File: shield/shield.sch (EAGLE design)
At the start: 23 parts, among them IC1 MCP2515-E/SO, IC2 MCP2562, IC3 LM2595NDH

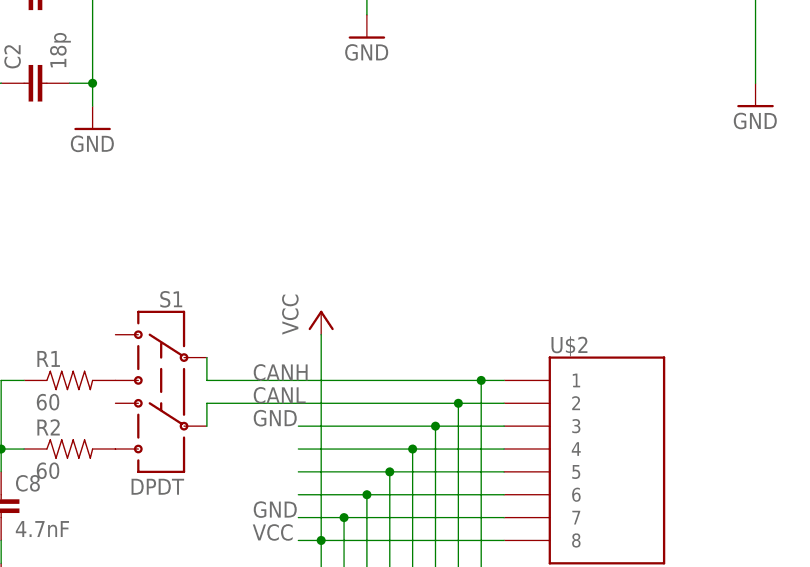
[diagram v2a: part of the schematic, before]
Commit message: Added TVS diodes, fixed silkscreen issues
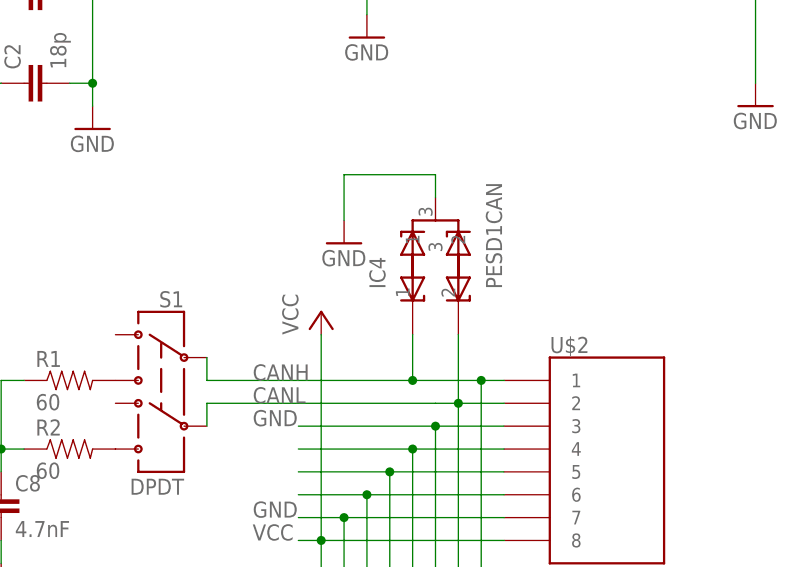
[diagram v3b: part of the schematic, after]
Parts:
- added IC4: PESD1CAN, nickparts:PESD1CAN
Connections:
- net CANH: now also IC4.1
- net CANL: now also IC4.2
- net GND: now also IC4.3
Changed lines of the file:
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@@
 <part name="C8" library="SparkFun-Passives" deviceset="CAP" device="0603-CAP" value="4.7nF"/>
 <part name="GND1" library="supply1" deviceset="GND" device=""/>
+<part name="IC4" library="nickparts" deviceset="PESD1CAN" device=""/>
+<part name="GND2" library="supply1" deviceset="GND" device=""/>
 </parts>
 <sheets>
@@
 <instance part="C8" gate="G$1" x="335.28" y="-88.9"/>
 <instance part="GND1" gate="1" x="335.28" y="-96.52"/>
+<instance part="IC4" gate="G$1" x="383.54" y="-55.88" rot="R90"/>
+<instance part="GND2" gate="1" x="373.38" y="-58.42"/>
 </instances>
 <busses>
@@
 <wire x1="335.28" y1="-91.44" x2="335.28" y2="-93.98" width="0.1524" layer="91"/>
 </segment>
+<segment>
+<pinref part="IC4" gate="G$1" pin="3"/>
+<wire x1="383.54" y1="-53.34" x2="383.54" y2="-50.8" width="0.1524" layer="91"/>
+<pinref part="GND2" gate="1" pin="GND"/>
+<wire x1="383.54" y1="-50.8" x2="373.38" y2="-50.8" width="0.1524" layer="91"/>
+<wire x1="373.38" y1="-50.8" x2="373.38" y2="-55.88" width="0.1524" layer="91"/>
+</segment>
 </net>
 <net name="N$6" class="0">
@@
 <pinref part="U$3" gate="G$1" pin="1"/>
 <wire x1="388.62" y1="-101.6" x2="391.16" y2="-101.6" width="0.1524" layer="91"/>
-<wire x1="388.62" y1="-73.66" x2="368.3" y2="-73.66" width="0.1524" layer="91"/>
+<wire x1="388.62" y1="-73.66" x2="381" y2="-73.66" width="0.1524" layer="91"/>
 <junction x="388.62" y="-73.66"/>
 <label x="363.22" y="-73.66" size="1.778" layer="95"/>
 <pinref part="S1" gate="G$1" pin="2"/>
+<wire x1="381" y1="-73.66" x2="368.3" y2="-73.66" width="0.1524" layer="91"/>
 <wire x1="368.3" y1="-73.66" x2="358.14" y2="-73.66" width="0.1524" layer="91"/>
 <wire x1="358.14" y1="-73.66" x2="358.14" y2="-71.12" width="0.1524" layer="91"/>
+<pinref part="IC4" gate="G$1" pin="1"/>
+<wire x1="381" y1="-68.58" x2="381" y2="-73.66" width="0.1524" layer="91"/>
+<junction x="381" y="-73.66"/>
 </segment>
 </net>
@@
 <pinref part="U$3" gate="G$1" pin="2"/>
 <wire x1="386.08" y1="-104.14" x2="391.16" y2="-104.14" width="0.1524" layer="91"/>
-<wire x1="386.08" y1="-76.2" x2="368.3" y2="-76.2" width="0.1524" layer="91"/>
+<wire x1="386.08" y1="-76.2" x2="383.54" y2="-76.2" width="0.1524" layer="91"/>
 <junction x="386.08" y="-76.2"/>
 <label x="363.22" y="-76.2" size="1.778" layer="95"/>
 <pinref part="S1" gate="G$1" pin="5"/>
+<wire x1="383.54" y1="-76.2" x2="368.3" y2="-76.2" width="0.1524" layer="91"/>
 <wire x1="368.3" y1="-76.2" x2="358.14" y2="-76.2" width="0.1524" layer="91"/>
 <wire x1="358.14" y1="-76.2" x2="358.14" y2="-78.74" width="0.1524" layer="91"/>
-</segment>
-</net>
+<pinref part="IC4" gate="G$1" pin="2"/>
+<wire x1="386.08" y1="-68.58" x2="386.08" y2="-76.2" width="0.1524" layer="91"/>
+</segment>
+</net>

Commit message: Minor changes to shield, rpi board, and cape
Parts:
- removed L1: MSS1260, nickparts:MSS1260
- added C10: 56u, nickparts:10SVP56M
- added C9: 10n, nickparts:C0805C103K5RACTU
- added I1: SRN8040-330M, nickparts:SRN8040-330M
- C3: value (none) -> 4.7u; device SparkFun-Capacitors:CAP_POLG -> nickparts:GRM31CR71H475KA12L
- C4: value (none) -> 1u; device SparkFun-Capacitors:CAP_POLE -> nickparts:GMK212B7105KG-T
- D1: value (none) -> B240A-13-F; device SparkFun-DiscreteSemi:DIODESMA-ALT -> nickparts:B240A-13-F
- IC3: value LM2595NDH -> LM22675MR-5.0/NOPB; device nickparts:LM2595NDH -> nickparts:LM22675MR-5.0/NOPB
- U$1: value ARDUINO_R3_ICSP -> ARDUINO_R3_ICSPNODIM; device adafruit:ARDUINO_R3_ICSP -> nickparts:ARDUINO_R3_ICSPNODIM
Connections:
- net N$1 renamed RXCAN
- removed net N$11: U$2.5, U$3.5
- removed net N$6: D1.C, IC3.OUT, L1.1
- new net N$9: U$2.3, U$3.3
- new net SWOUT: C9.2, D1.K, I1.2, IC3.SW
- net +5V: now also C10.+, I1.1; no longer C4.+, L1.2
- net GND: now also C10.-, C3.2, C4.2, U$2.8, U$3.8; no longer C3.-, C4.-, IC3./EN, U$2.3, U$3.3
- net N$10: now also C9.1, IC3.BOOT; no longer U$2.4, U$3.4
- net VCC: now also C3.1, C4.1, U$2.4, U$2.5, U$3.4, U$3.5; no longer C3.+, U$2.8, U$3.8
